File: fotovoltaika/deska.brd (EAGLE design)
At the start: 100 x 80 mm, 19 parts

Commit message: upravy desek
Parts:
- removed R1, R11, R2, R3, R4, R5, R6, R7, R8, R9: (no value), rcl:0207/7
- removed X1, X2, X3, X4: (no value), con-wago-508:W237-132
- added SL3, SL4: (no value), con-amp-quick:04P
- added SUPPLY: (no value), con-wago-508:W237-132
- SL1: device con-amp-quick:10P -> con-amp-quick:04P
- moved SL1 42.8 mm to (35.6, 19.1), turned to 90 degrees
- moved WEMOS1 41.0 mm to (14.0, 20.3)
- moved SL2 35.0 mm to (31.8, 19.1), turned to 90 degrees
- moved R10 33.8 mm to (21.6, 10.2), turned to 270 degrees
- moved LED 21.9 mm to (38.1, 6.35)
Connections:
- removed net N$10: R4.2, X4.1
- removed net N$13: R11.2, R9.1, WEMOS1.D7
- removed net N$3: R1.2, X1.1
- removed net N$4: R1.1, R5.2, SL1.1
- removed net N$5: R2.1, R6.2, SL1.2
- removed net N$6: R3.1, R7.2, SL1.3
- removed net N$7: R4.1, R8.2, SL1.4
- removed net N$8: R2.2, X2.1
- removed net N$9: R3.2, X3.1
- net +5V: now also SL1.1, SL3.1, SL4.1, SUPPLY.2; no longer SL1.10
- net GND: now also SL1.2, SL3.2, SL4.2, SUPPLY.1; no longer R11.1, R5.1, R6.1, R7.1, R8.1, SL1.6, SL1.9, X1.2, X2.2, X3.2, X4.2
- net N$1: now also SL1.4, SL2.4, SL3.4, SL4.4, WEMOS1.D1; no longer SL1.7, WEMOS1.D2
- net N$2: now also SL1.3, SL2.3, SL3.3, SL4.3, WEMOS1.D2; no longer SL1.8, WEMOS1.D1
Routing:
- net +5V: track 6.35 -> 93.4 mm
- net GND: track 127.8 -> 62.3 mm
- net N$10: track 42.9 -> 0.00 mm
- net N$9: track 30.9 -> 0.00 mm
- net N$4: track 22.9 -> 0.00 mm
- net N$8: track 18.2 -> 0.00 mm
- net N$5: track 17.8 -> 0.00 mm
- net N$2: track 0.00 -> 16.5 mm
- net N$12: track 0.00 -> 14.2 mm
- net N$6: track 12.7 -> 0.00 mm
- net N$3: track 10.6 -> 0.00 mm
- net N$1: track 7.40 -> 16.5 mm
- net N$7: track 7.62 -> 0.00 mm
- net N$11: track 0.00 -> 5.08 mm
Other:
- board size 100 x 80 mm -> 46.7 x 36.8 mm

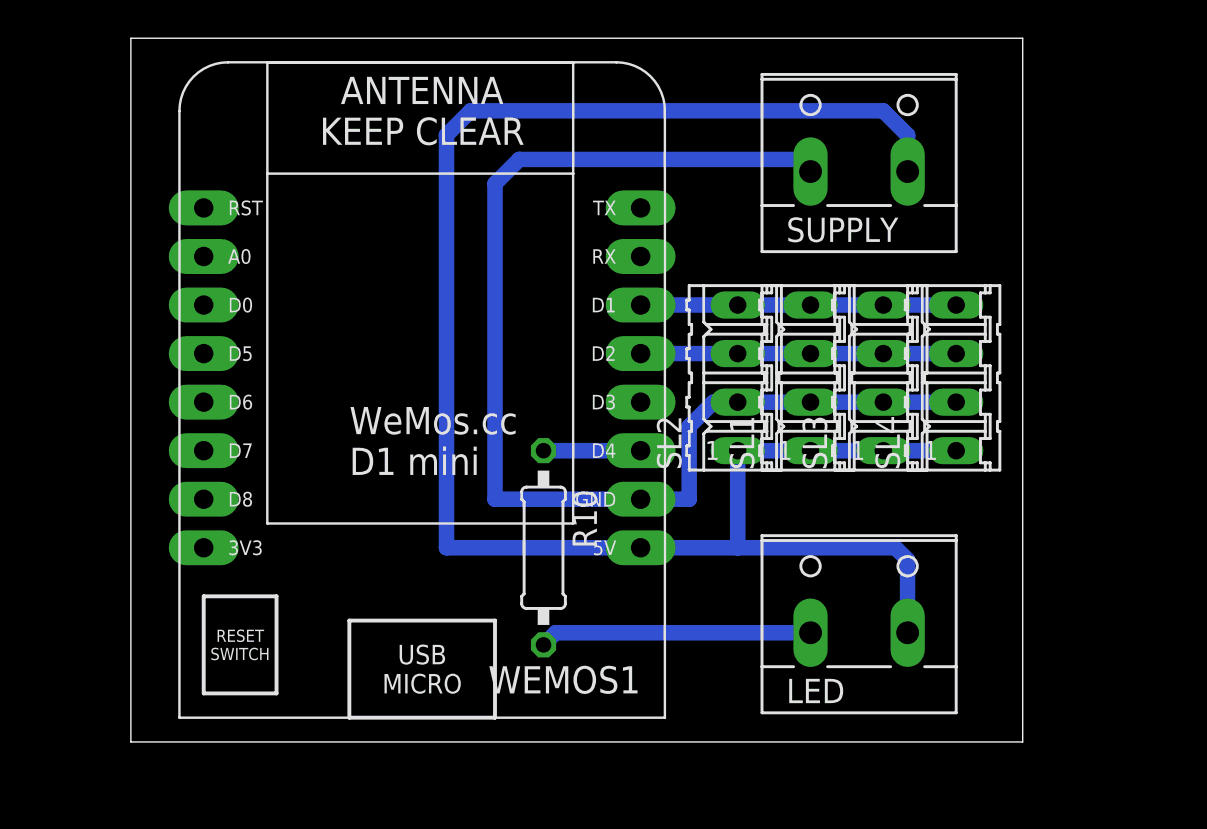
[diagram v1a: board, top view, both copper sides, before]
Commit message: uprava desky ovladani rele
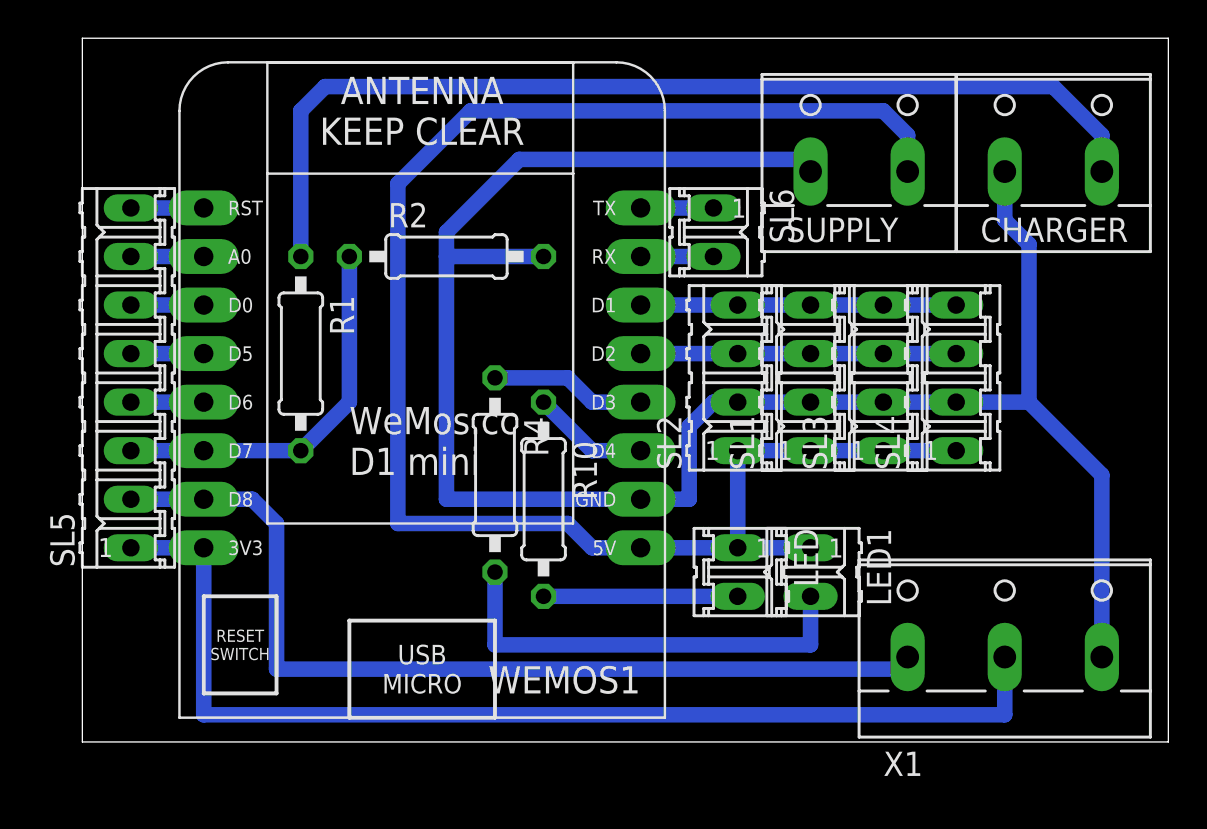
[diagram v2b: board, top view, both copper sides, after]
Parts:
- added CHARGER: (no value), con-wago-508:W237-132
- added LED1, SL6: (no value), con-amp-quick:02P
- added R1: 10k, rcl:0207/10
- added R2: 2k7, rcl:0207/10
- added R4: 220, rcl:0207/10
- added SL5: (no value), con-amp-quick:08P
- added X1: (no value), con-wago-508:W237-3E
- LED: device con-wago-508:W237-132 -> con-amp-quick:02P
- moved LED 6.84 mm to (31.8, 8.89), turned to 270 degrees
- moved R10 2.54 mm to (21.6, 12.7)
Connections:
- new net N$10: R1.2, R2.1, SL5.3, WEMOS1.D7
- new net N$13: SL5.8, WEMOS1.RESET
- new net N$14: SL6.1, WEMOS1.TX
- new net N$15: SL6.2, WEMOS1.RX
- new net N$16: LED1.2, R4.2
- new net N$17: R4.1, WEMOS1.D3
- new net N$18: SL5.1, WEMOS1.3V3, X1.2
- new net N$3: SL5.7, WEMOS1.A0
- new net N$4: SL5.2, WEMOS1.D8, X1.1
- new net N$5: CHARGER.2, R1.1
- new net N$7: SL5.4, WEMOS1.D6
- new net N$8: SL5.5, WEMOS1.D5
- new net N$9: SL5.6, WEMOS1.D0
- net +5V: now also LED.1, LED1.1; no longer LED.2
- net GND: now also CHARGER.1, R2.2, X1.3
- net N$12: now also LED.2; no longer LED.1
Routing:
- net N$18: track 0.00 -> 57.5 mm
- net N$5: track 0.00 -> 53.0 mm
- net N$4: track 0.00 -> 49.0 mm
- net GND: track 62.3 -> 102.3 mm
- net N$16: track 0.00 -> 22.9 mm
- net N$10: track 0.00 -> 20.1 mm
- net N$17: track 0.00 -> 8.15 mm
- net +5V: track 93.4 -> 87.1 mm
- net N$12: track 14.2 -> 10.2 mm
- net N$9: track 0.00 -> 3.81 mm
- net N$8: track 0.00 -> 3.81 mm
- net N$7: track 0.00 -> 3.81 mm
- net N$3: track 0.00 -> 3.81 mm
- net N$13: track 0.00 -> 3.81 mm
- net N$15: track 0.00 -> 3.81 mm
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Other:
- board size 46.7 x 36.8 mm -> 56.8 x 36.8 mm

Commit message: uprava desky
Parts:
- removed SL1, SL2: (no value), con-amp-quick:04P
- added DISPLAY, INA219: (no value), con-amp-quick:04P
- moved SL3 2.54 mm to (41.9, 19.1)
- moved SL4 1.27 mm to (44.5, 19.1)
- renumbered SL6 to MODEM, X1 to RELAY
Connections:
- net N$18 renamed +3V3
- net +5V: now also DISPLAY.1, INA219.1; no longer SL1.1, SL2.1
- net GND: now also DISPLAY.2, INA219.2; no longer SL1.2, SL2.2
- net N$1: now also DISPLAY.4, INA219.4; no longer SL1.4, SL2.4
- net N$2: now also DISPLAY.3, INA219.3; no longer SL1.3, SL2.3
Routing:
- net N$4: track 49.0 -> 51.6 mm
- net +3V3: track 57.5 -> 60.0 mm
- net GND: track 102.3 -> 104.3 mm
- net N$2: track 16.5 -> 17.8 mm
- net N$1: track 16.5 -> 17.8 mm
- net +5V: track 87.1 -> 88.4 mm
- net N$5: track 53.0 -> 54.1 mm
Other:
- board size 56.8 x 36.8 mm -> 61.9 x 44.4 mm

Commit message: zmena odporu delice
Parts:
- R2: value 2k7 -> 2k2
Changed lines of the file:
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@@
 <?xml version="1.0" encoding="utf-8"?>
 <!DOCTYPE eagle SYSTEM "eagle.dtd">
-<eagle version="9.4.1">
+<eagle version="9.3.0">
 <drawing>
 <settings>
@@
 <attribute name="VALUE" x="34.29" y="23.495" size="1.27" layer="27" ratio="10"/>
 </element>
-<element name="R1" library="rcl" package="0207/10" override_package3d_urn="urn:adsk.eagle:package:11209799/2" override_package_urn="urn:adsk.eagle:footprint:11209800/1" value="10k" x="8.89" y="20.32" smashed="yes" rot="R270">
+<element name="R1" library="rcl" package="0207/10" value="10k" x="8.89" y="20.32" smashed="yes" rot="R270">
 <attribute name="NAME" x="10.414" y="23.368" size="1.27" layer="25" ratio="10" rot="R270"/>
 <attribute name="VALUE" x="8.255" y="22.5806" size="1.27" layer="27" ratio="10" rot="R270"/>
 </element>
-<element name="R2" library="rcl" package="0207/10" override_package3d_urn="urn:adsk.eagle:package:11209793/2" override_package_urn="urn:adsk.eagle:footprint:11209794/1" value="2k7" x="16.51" y="25.4" smashed="yes">
+<element name="R2" library="rcl" package="0207/10" value="2k2" x="16.51" y="25.4" smashed="yes">
 <attribute name="NAME" x="13.462" y="26.924" size="1.27" layer="25" ratio="10"/>
 <attribute name="VALUE" x="14.2494" y="24.765" size="1.27" layer="27" ratio="10"/>
@@
 packages will not be understood (or retained) with this version.
 </note>
-<note version="9.4" severity="warning">
-Since Version 9.4, EAGLE supports the overriding of 3D packages
-in schematics and board files. Those overridden 3d packages
-will not be understood (or retained) with this version.
-</note>
 </compatibility>
